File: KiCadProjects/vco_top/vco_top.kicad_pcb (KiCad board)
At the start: 2 copper layers, 160 x 100 mm, 22 parts, among them J1 Mono_Jack_112APCX, J2 Mono_Jack_112APCX, J3 Mono_Jack_112APCX, J4 Mono_Jack_112APCX, J5 Mono_Jack_112APCX, J6 Mono_Jack_112APCX, P1 100k, P2 100k, P3 100k, P4 100k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

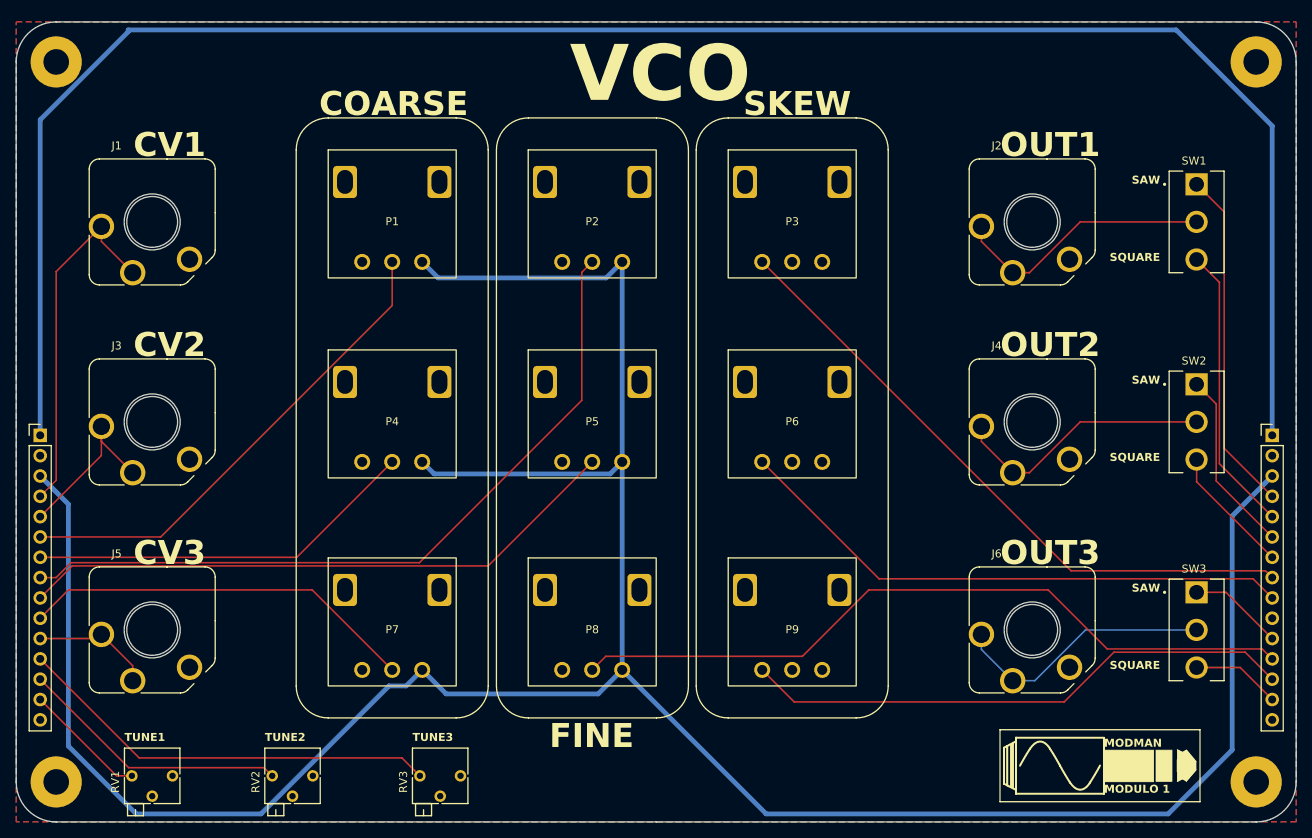
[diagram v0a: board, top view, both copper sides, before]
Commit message: added vco top and bottom
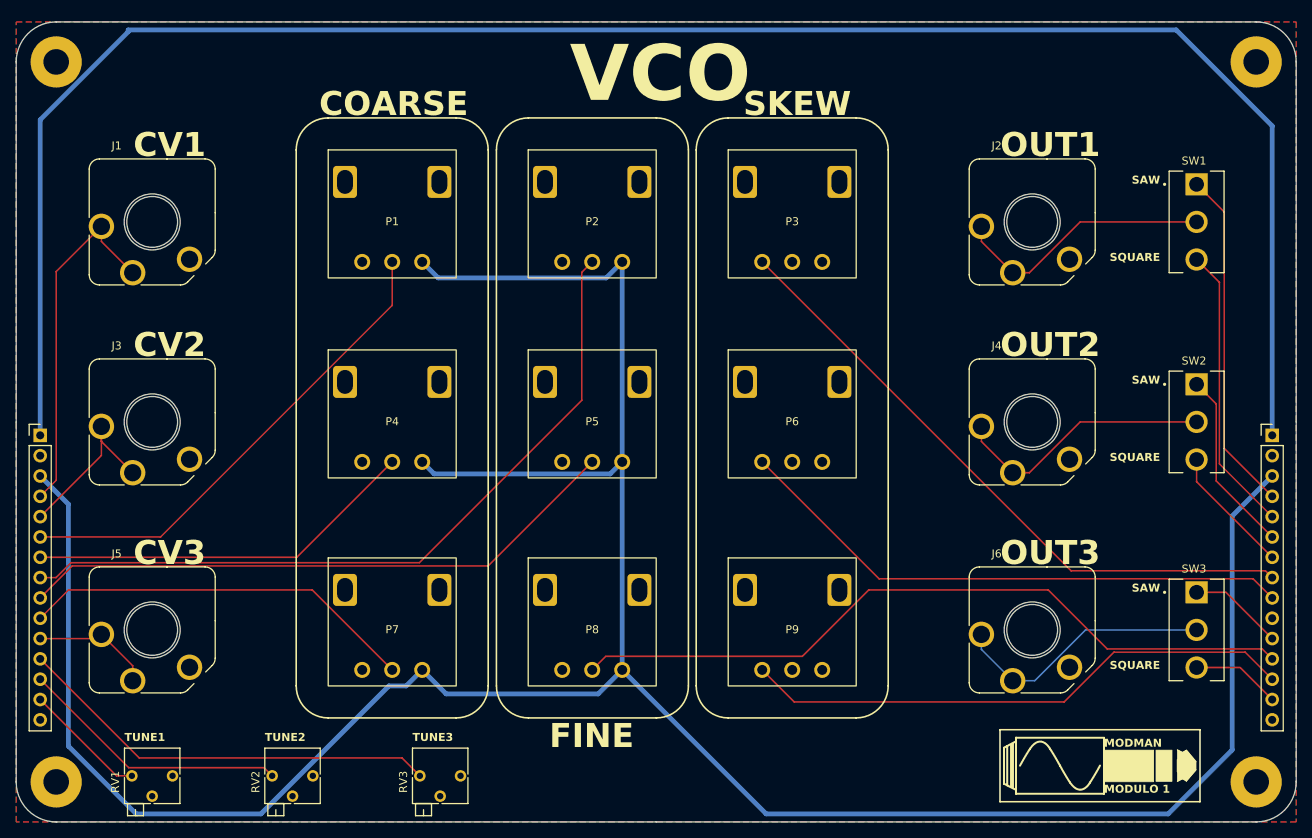
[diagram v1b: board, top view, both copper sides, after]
